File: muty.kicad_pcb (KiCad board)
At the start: 4 copper layers, 68 parts, among them J1 Conn_ARM_SWD_TagConnect_TC2030, J2 Conn_02x05_Odd_Even, U1 STM32F439ZITx, U2 BME280, U3 BNO085, U4 TB6612FNG, U5 TB6612FNG, Y1 ECS-2520MVQ-160-CN-TR, Y2 NX3215SA-32.768KHZ-EXS00A-MU0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, Y3 NX3215SA-32.768KHZ-EXS00A-MU0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

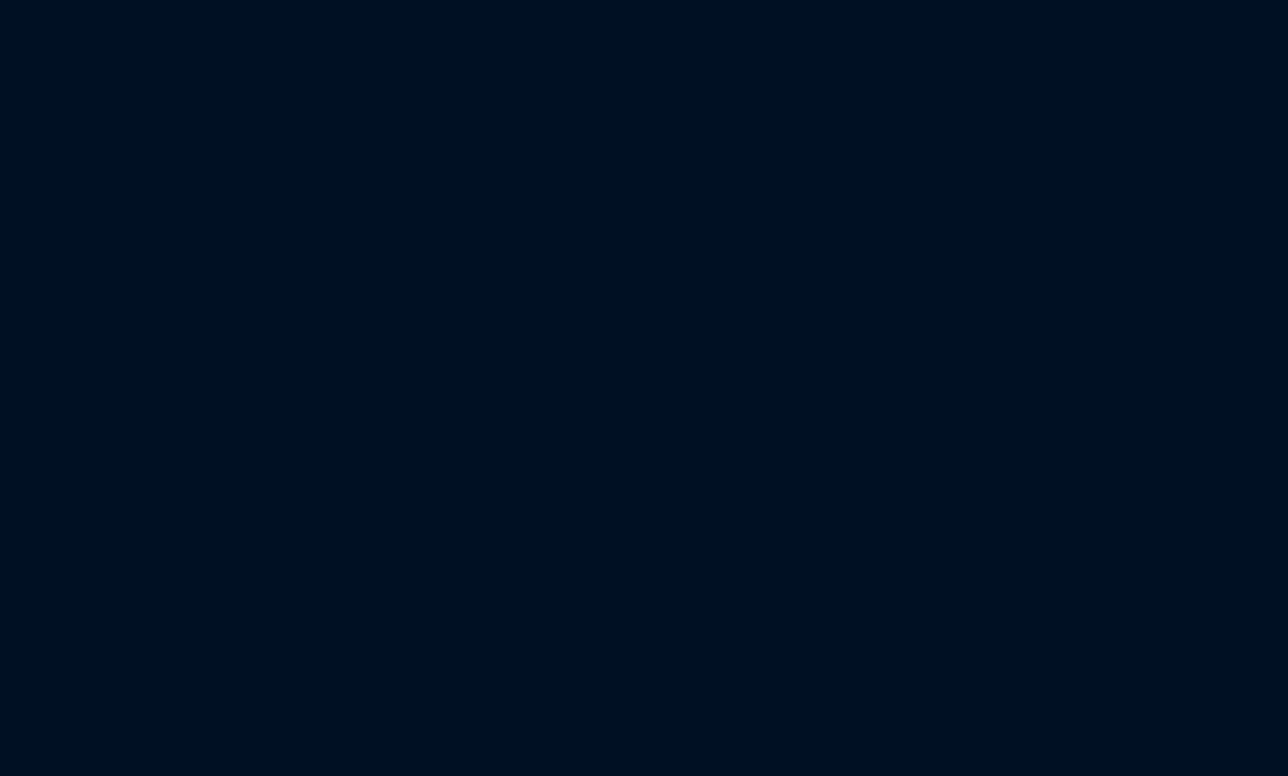
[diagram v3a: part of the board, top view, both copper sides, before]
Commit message: feat: add ethernet
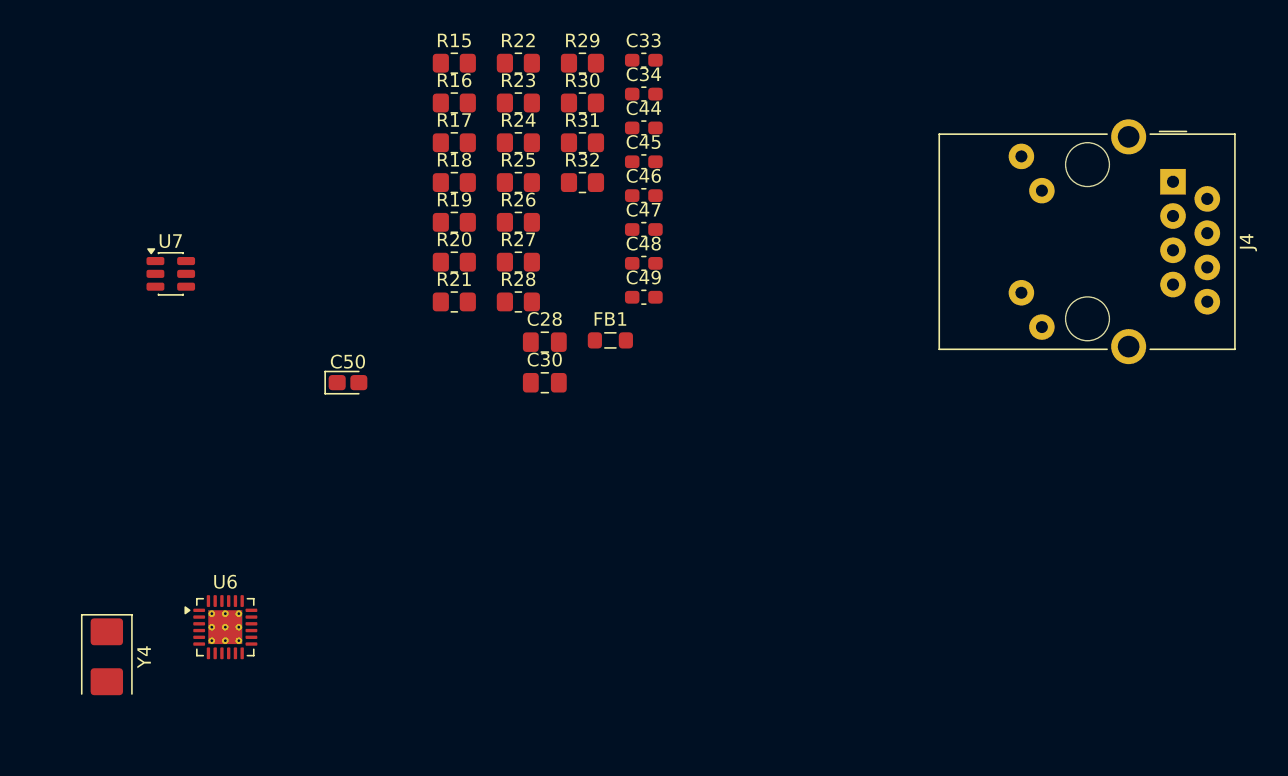
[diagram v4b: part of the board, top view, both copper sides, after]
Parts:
- added C28: 30pF, Capacitor_SMD:C_0805_2012Metric_Pad1.18x1.45mm_HandSolder, F.Cu at (203.6, 37.7)
- added C30: 30pF, Capacitor_SMD:C_0805_2012Metric_Pad1.18x1.45mm_HandSolder, F.Cu at (203.6, 40.8)
- added C33: 100nF, Capacitor_SMD:C_0603_1608Metric_Pad1.08x0.95mm_HandSolder, F.Cu at (210.9, 16.8)
- added C34: 470pF, Capacitor_SMD:C_0603_1608Metric_Pad1.08x0.95mm_HandSolder, F.Cu at (210.9, 19.4)
- added C44: 1uF_X5R, Capacitor_SMD:C_0603_1608Metric_Pad1.08x0.95mm_HandSolder, F.Cu at (210.9, 21.9)
- added C45: 100nF, Capacitor_SMD:C_0603_1608Metric_Pad1.08x0.95mm_HandSolder, F.Cu at (210.9, 24.4)
- added C46: 100nF, Capacitor_SMD:C_0603_1608Metric_Pad1.08x0.95mm_HandSolder, F.Cu at (210.9, 26.9)
- added C47: 100nF, Capacitor_SMD:C_0603_1608Metric_Pad1.08x0.95mm_HandSolder, F.Cu at (210.9, 29.4)
- added C48: 100nF, Capacitor_SMD:C_0603_1608Metric_Pad1.08x0.95mm_HandSolder, F.Cu at (210.9, 31.9)
- added C49: 100nF, Capacitor_SMD:C_0603_1608Metric_Pad1.08x0.95mm_HandSolder, F.Cu at (210.9, 34.4)
- added C50: 10μF, Capacitor_Tantalum_SMD:CP_EIA-1608-10_AVX-L_HandSolder, F.Cu at (189.0, 40.7)
- added FB1: FerriteBead, Inductor_SMD:L_0805_2012Metric_Pad1.05x1.20mm_HandSolder, F.Cu at (208.4, 37.6)
- added J4: RJ45_Amphenol_RJMG1BD3B8K1ANR, Connector_RJ:RJ45_Amphenol_RJMG1BD3B8K1ANR, F.Cu at (250.1, 25.9)
- added R15: 10K, Resistor_SMD:R_0805_2012Metric_Pad1.20x1.40mm_HandSolder, F.Cu at (196.8, 17.1)
- added R16: 10K, Resistor_SMD:R_0805_2012Metric_Pad1.20x1.40mm_HandSolder, F.Cu at (196.8, 20.0)
- added R17: 10K, Resistor_SMD:R_0805_2012Metric_Pad1.20x1.40mm_HandSolder, F.Cu at (196.8, 23.0)
- added R18: 33, Resistor_SMD:R_0805_2012Metric_Pad1.20x1.40mm_HandSolder, F.Cu at (196.8, 25.9)
- added R19: 33, Resistor_SMD:R_0805_2012Metric_Pad1.20x1.40mm_HandSolder, F.Cu at (196.8, 28.9)
- added R20: 33, Resistor_SMD:R_0805_2012Metric_Pad1.20x1.40mm_HandSolder, F.Cu at (196.8, 31.8)
- added R21: 10K, Resistor_SMD:R_0805_2012Metric_Pad1.20x1.40mm_HandSolder, F.Cu at (196.8, 34.8)
- added R22: 33, Resistor_SMD:R_0805_2012Metric_Pad1.20x1.40mm_HandSolder, F.Cu at (201.6, 17.1)
- added R23: 10K, Resistor_SMD:R_0805_2012Metric_Pad1.20x1.40mm_HandSolder, F.Cu at (201.6, 20.0)
- added R24: 1.5K, Resistor_SMD:R_0805_2012Metric_Pad1.20x1.40mm_HandSolder, F.Cu at (201.6, 23.0)
- added R25: 50, Resistor_SMD:R_0805_2012Metric_Pad1.20x1.40mm_HandSolder, F.Cu at (201.6, 25.9)
- added R26: 10K, Resistor_SMD:R_0805_2012Metric_Pad1.20x1.40mm_HandSolder, F.Cu at (201.6, 28.9)
- added R27: 50, Resistor_SMD:R_0805_2012Metric_Pad1.20x1.40mm_HandSolder, F.Cu at (201.6, 31.8)
- added R28: 50, Resistor_SMD:R_0805_2012Metric_Pad1.20x1.40mm_HandSolder, F.Cu at (201.6, 34.8)
- added R29: 50, Resistor_SMD:R_0805_2012Metric_Pad1.20x1.40mm_HandSolder, F.Cu at (206.3, 17.1)
- added R30: 270, Resistor_SMD:R_0805_2012Metric_Pad1.20x1.40mm_HandSolder, F.Cu at (206.3, 20.0)
- added R31: 270, Resistor_SMD:R_0805_2012Metric_Pad1.20x1.40mm_HandSolder, F.Cu at (206.3, 23.0)
- added R32: 10K, Resistor_SMD:R_0805_2012Metric_Pad1.20x1.40mm_HandSolder, F.Cu at (206.3, 25.9)
- added U6: LAN8742A-CZ-TR, Package_DFN_QFN:VQFN-24-1EP_4x4mm_P0.5mm_EP2.5x2.5mm_ThermalVias, F.Cu at (179.9, 58.9)
- added U7: USBLC6-4SC6, Package_TO_SOT_SMD:SOT-23-6, F.Cu at (175.8, 32.7)
- added Y4: X53T-C20SSA-25.000MHz, Crystal:Crystal_SMD_5032-2Pin_5.0x3.2mm, F.Cu at (171.1, 61.1)
